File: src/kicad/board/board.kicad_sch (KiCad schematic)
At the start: 20 parts, among them J1 USB_C_Receptacle_USB2.0, J2 Conn_01x06, J3 Micro_SD_Card_Det

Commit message: update, schematic should be done
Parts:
- added H1, H2, H3, H4: MountingHole, MountingHole:MountingHole_3.2mm_M3_DIN965_Pad, symbol Mechanical:MountingHole
- R3, R4, R5, R6, R7, R8: value 47K -> 10K; footprint Resistor_SMD:R_0805_2012Metric -> Resistor_SMD:R_0603_1608Metric; Vendor C17713 -> C25804
- gave numbers to parts that had none: 5
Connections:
- net +3.3V: no longer R5.1
- net GND: now also R5.2
- net SD_CLK: now also R5.1; no longer R5.2
- net SD_DAT2: now reaches J3.1 (DAT2), R8.2
- net SD_DAT1: now reaches J3.8 (DAT1), R3.2
- no-connect marks 16 -> 18
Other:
- moved on the sheet: C1, C2, R3, R4, R5, R6, R7, R8

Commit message: wip
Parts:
- C1: footprint Capacitor_SMD:C_0805_2012Metric -> Capacitor_SMD:C_0603_1608Metric; Vendor C15850 -> C19702
- C2: value 0.1uF -> 100nF; footprint Capacitor_SMD:C_0805_2012Metric -> Capacitor_SMD:C_0603_1608Metric; Vendor C28233 -> C14663
- R1, R2: footprint Resistor_SMD:R_0805_2012Metric -> Resistor_SMD:R_0603_1608Metric; Vendor C27834 -> C23186
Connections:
- net rp2040/GPIO12: now also J2.1 (Pin_1)
- net rp2040/GPIO13: now also J2.2 (Pin_2)
- net rp2040/GPIO14: now also J2.3 (Pin_3)
- net rp2040/GPIO15: now also J2.4 (Pin_4)
- net rp2040/GPIO16: now also J2.5 (Pin_5); no longer J2.1 (Pin_1)
- net rp2040/GPIO17: now also J2.6 (Pin_6); no longer J2.2 (Pin_2)
- net rp2040/GPIO18: no longer J2.3 (Pin_3)
- net rp2040/GPIO19: no longer J2.4 (Pin_4)
- net rp2040/GPIO20: no longer J2.5 (Pin_5)
- net rp2040/GPIO21: no longer J2.6 (Pin_6)
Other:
- sheet Sound ports: added BLCK, DIN, LRCLK; removed none
- moved on the sheet: H1, H2, H3, H4, J2

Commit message: update
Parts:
- C2: footprint Capacitor_SMD:C_0603_1608Metric -> Capacitor_SMD:C_0402_1005Metric; Vendor C14663 -> C307331
- R10, R9: footprint Resistor_SMD:R_0805_2012Metric -> Resistor_SMD:R_0603_1608Metric; Vendor C17594 -> C25190
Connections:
- net rp2040/GPIO12: no longer J2.1 (Pin_1)
- net rp2040/GPIO13: no longer J2.2 (Pin_2)
- net rp2040/GPIO14: no longer J2.3 (Pin_3)
- net rp2040/GPIO15: no longer J2.4 (Pin_4)
- net rp2040/GPIO16: no longer J2.5 (Pin_5)
- net rp2040/GPIO17: no longer J2.6 (Pin_6)
- no-connect marks 18 -> 6
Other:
- moved on the sheet: J2

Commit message: update
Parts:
- removed J2: Conn_01x06, Connector_PinHeader_2.54mm:PinHeader_1x06_P2.54mm_Vertical, symbol Connector_Generic:Conn_01x06
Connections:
- no-connect marks 6 -> 24
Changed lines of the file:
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@@
   (junction (at 77.47 137.16) (diameter 0) (color 0 0 0 0)
   )
+  (no_connect (at 111.76 109.22))
+  (no_connect (at 148.59 58.42))
   (no_connect (at 81.28 173.99))
+  (no_connect (at 111.76 101.6))
   (no_connect (at 129.54 48.26))
+  (no_connect (at 148.59 83.82))
+  (no_connect (at 148.59 81.28))
   (no_connect (at 81.28 176.53))
+  (no_connect (at 111.76 111.76))
+  (no_connect (at 111.76 106.68))
+  (no_connect (at 148.59 63.5))
+  (no_connect (at 111.76 104.14))
+  (no_connect (at 148.59 55.88))
+  (no_connect (at 111.76 99.06))
+  (no_connect (at 148.59 73.66))
+  (no_connect (at 148.59 66.04))
   (no_connect (at 52.07 69.85))
+  (no_connect (at 148.59 78.74))
+  (no_connect (at 148.59 60.96))
+  (no_connect (at 148.59 76.2))
   (no_connect (at 127 48.26))
+  (no_connect (at 148.59 68.58))
   (no_connect (at 52.07 72.39))
+  (no_connect (at 148.59 71.12))
   (wire (pts (xy 106.68 71.12) (xy 111.76 71.12))
     (stroke (width 0) (type default) (color 0 0 0 0))
@@
     (pin "1")
     (pin "2")
-  )
-  (symbol (lib_id "Connector_Generic:Conn_01x06") (at 100.33 110.49 180) (unit 1)
-    (in_bom yes) (on_board yes)
-    (property "Reference" "J2" (id 0) (at 95.25 105.41 0))
-    (property "Value" "Conn_01x06" (id 1) (at 92.71 107.95 0))
-    (property "Footprint" "Connector_PinHeader_2.54mm:PinHeader_1x06_P2.54mm_Vertical" (id 2) (at 100.33 110.49 0)
-      (effects (font (size 1.27 1.27)) hide)
-    )
-    (property "Datasheet" "~" (id 3) (at 100.33 110.49 0)
-      (effects (font (size 1.27 1.27)) hide)
-    )
-    (pin "1")
-    (pin "2")
-    (pin "3")
-    (pin "4")
-    (pin "5")
-    (pin "6")
   )
   (symbol (lib_id "power:+3.3V") (at 195.58 114.3 0) (unit 1)
@@
       (reference "D5") (unit 1) (value "CHARGE_LED") (footprint "LED_SMD:LED_0805_2012Metric")
     )
-    (path "/d540bb9b-d45f-4ddd-b651-2c00d8abffca/7217d876-f1ed-4bca-b991-1e14633870a6"
-      (reference "FB1") (unit 1) (value "Ferrite") (footprint "Library:Ferrite-0805")
-    )
-    (path "/d540bb9b-d45f-4ddd-b651-2c00d8abffca/c0f8ca9a-4e15-418c-8a7f-48417a436431"
-      (reference "FB2") (unit 1) (value "Ferrite") (footprint "Library:Ferrite-0805")
-    )
     (path "/0b29145a-63e8-45a2-940d-9799db9d94f0"
       (reference "H1") (unit 1) (value "MountingHole") (footprint "MountingHole:MountingHole_3.2mm_M3_DIN965_Pad")
@@
       (reference "J1") (unit 1) (value "USB_C_Receptacle_USB2.0") (footprint "Connector_USB:USB_C_Receptacle_G-Switch_GT-USB-7010ASV")
     )
-    (path "/4de2f5e7-d335-4195-9642-413a4a312947"
-      (reference "J2") (unit 1) (value "Conn_01x06") (footprint "Connector_PinHeader_2.54mm:PinHeader_1x06_P2.54mm_Vertical")
-    )
     (path "/6374251b-7a4e-4399-bc11-b4640567a0db"

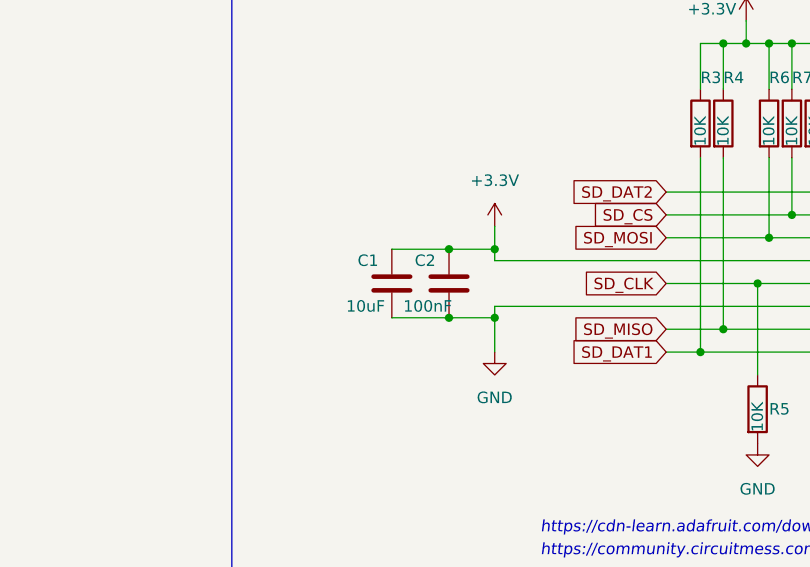
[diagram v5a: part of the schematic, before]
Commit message: separate io board from main
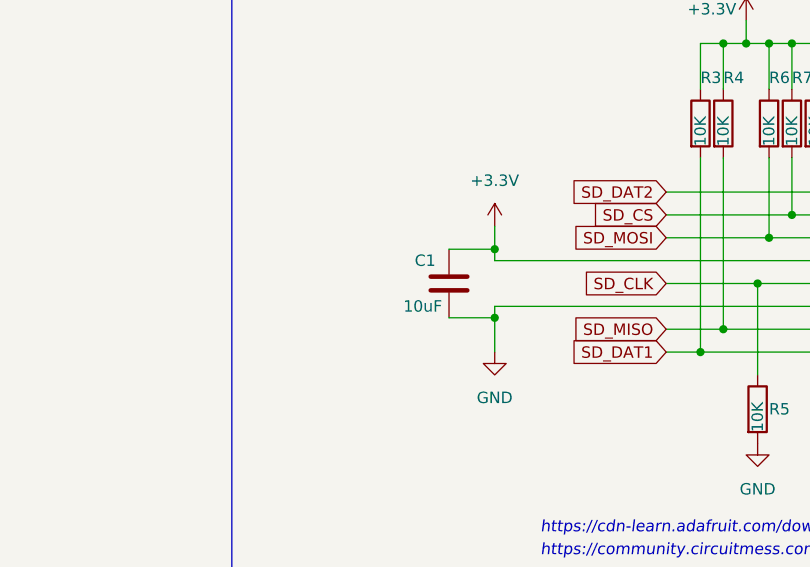
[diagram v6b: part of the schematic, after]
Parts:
- removed C2: 100nF, Capacitor_SMD:C_0402_1005Metric, symbol Device:C
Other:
- moved on the sheet: C1
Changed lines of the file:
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@@
 (kicad_sch (version 20211123) (generator eeschema)
   (paper "A4")
-  (junction (at 39.37 160.02) (diameter 0) (color 0 0 0 0)
-  )
   (junction (at 74.93 81.28) (diameter 0) (color 0 0 0 0)
   )
@@
   )
   (junction (at 29.21 82.55) (diameter 0) (color 0 0 0 0)
-  )
-  (junction (at 39.37 167.64) (diameter 0) (color 0 0 0 0)
   )
   (junction (at 44.45 167.64) (diameter 0) (color 0 0 0 0)
@@
     (stroke (width 0) (type default) (color 0 0 0 0))
   )
-  (wire (pts (xy 33.02 160.02) (xy 39.37 160.02))
-    (stroke (width 0) (type default) (color 0 0 0 0))
-  )
   (wire (pts (xy 93.98 62.23) (xy 111.76 62.23))
     (stroke (width 0) (type default) (color 0 0 0 0))
@@
   )
   (wire (pts (xy 236.22 114.3) (xy 238.76 114.3))
-    (stroke (width 0) (type default) (color 0 0 0 0))
-  )
-  (wire (pts (xy 33.02 167.64) (xy 39.37 167.64))
     (stroke (width 0) (type default) (color 0 0 0 0))
   )
@@
       (effects (font (size 1.27 1.27)) hide)
     )
-  )
-  (symbol (lib_id "Device:C") (at 39.37 163.83 0) (unit 1)
-    (in_bom yes) (on_board yes)
-    (property "Reference" "C2" (id 0) (at 35.56 161.29 0)
-      (effects (font (size 1.27 1.27)) (justify left))
-    )
-    (property "Value" "100nF" (id 1) (at 34.29 166.37 0)
-      (effects (font (size 1.27 1.27)) (justify left))
-    )
-    (property "Footprint" "Capacitor_SMD:C_0402_1005Metric" (id 2) (at 40.3352 167.64 0)
-      (effects (font (size 1.27 1.27)) hide)
-    )
-    (property "Datasheet" "~" (id 3) (at 39.37 163.83 0)
-      (effects (font (size 1.27 1.27)) hide)
-    )
-    (property "Vendor" "C307331" (id 4) (at 39.37 163.83 0)
-      (effects (font (size 1.27 1.27)) hide)
-    )
-    (pin "1")
-    (pin "2")
   )
   (symbol (lib_id "Device:R") (at 73.66 177.8 0) (unit 1)
@@
     (pin "1")
   )
-  (symbol (lib_id "Device:C") (at 33.02 163.83 0) (unit 1)
-    (in_bom yes) (on_board yes)
-    (property "Reference" "C1" (id 0) (at 29.21 161.29 0)
-      (effects (font (size 1.27 1.27)) (justify left))
-    )
-    (property "Value" "10uF" (id 1) (at 27.94 166.37 0)
-      (effects (font (size 1.27 1.27)) (justify left))
-    )
-    (property "Footprint" "Capacitor_SMD:C_0603_1608Metric" (id 2) (at 33.9852 167.64 0)
-      (effects (font (size 1.27 1.27)) hide)
-    )
-    (property "Datasheet" "~" (id 3) (at 33.02 163.83 0)
-      (effects (font (size 1.27 1.27)) hide)
-    )
-    (property "Vendor" "C19702" (id 4) (at 33.02 163.83 0)
+  (symbol (lib_id "Device:C") (at 39.37 163.83 0) (unit 1)
+    (in_bom yes) (on_board yes)
+    (property "Reference" "C1" (id 0) (at 35.56 161.29 0)
+      (effects (font (size 1.27 1.27)) (justify left))
+    )
+    (property "Value" "10uF" (id 1) (at 34.29 166.37 0)
+      (effects (font (size 1.27 1.27)) (justify left))
+    )
+    (property "Footprint" "Capacitor_SMD:C_0603_1608Metric" (id 2) (at 40.3352 167.64 0)
+      (effects (font (size 1.27 1.27)) hide)
+    )
+    (property "Datasheet" "~" (id 3) (at 39.37 163.83 0)
+      (effects (font (size 1.27 1.27)) hide)
+    )
+    (property "Vendor" "C19702" (id 4) (at 39.37 163.83 0)
       (effects (font (size 1.27 1.27)) hide)
     )
@@
       (reference "C1") (unit 1) (value "10uF") (footprint "Capacitor_SMD:C_0603_1608Metric")
     )
-    (path "/1b30703b-465f-4cce-94e8-92560a46498a"
-      (reference "C2") (unit 1) (value "100nF") (footprint "Capacitor_SMD:C_0402_1005Metric")
-    )
     (path "/792c0ba8-28d7-4e30-aff1-9f3fa34c73f6/1dc6a10f-ec56-4ffc-9d20-6da7a3305ac3"

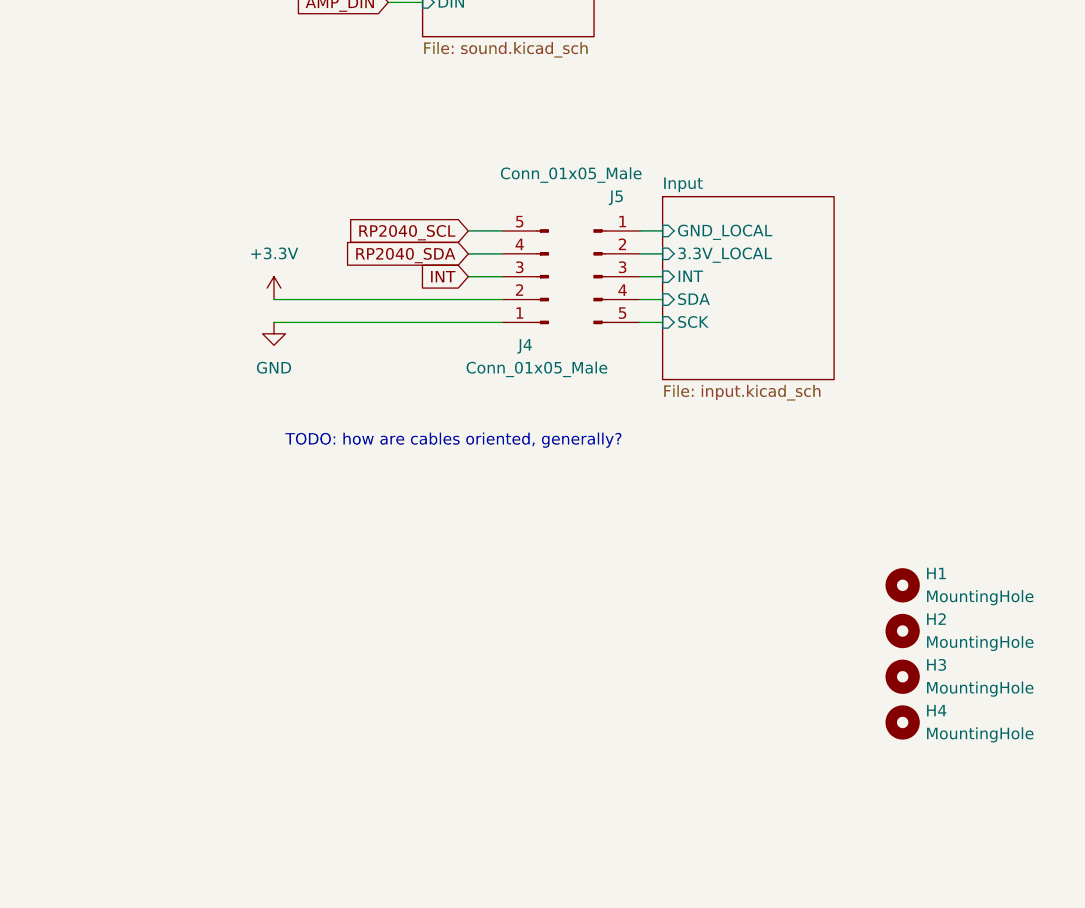
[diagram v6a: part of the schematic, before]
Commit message: remove io-board stuff from the main board project
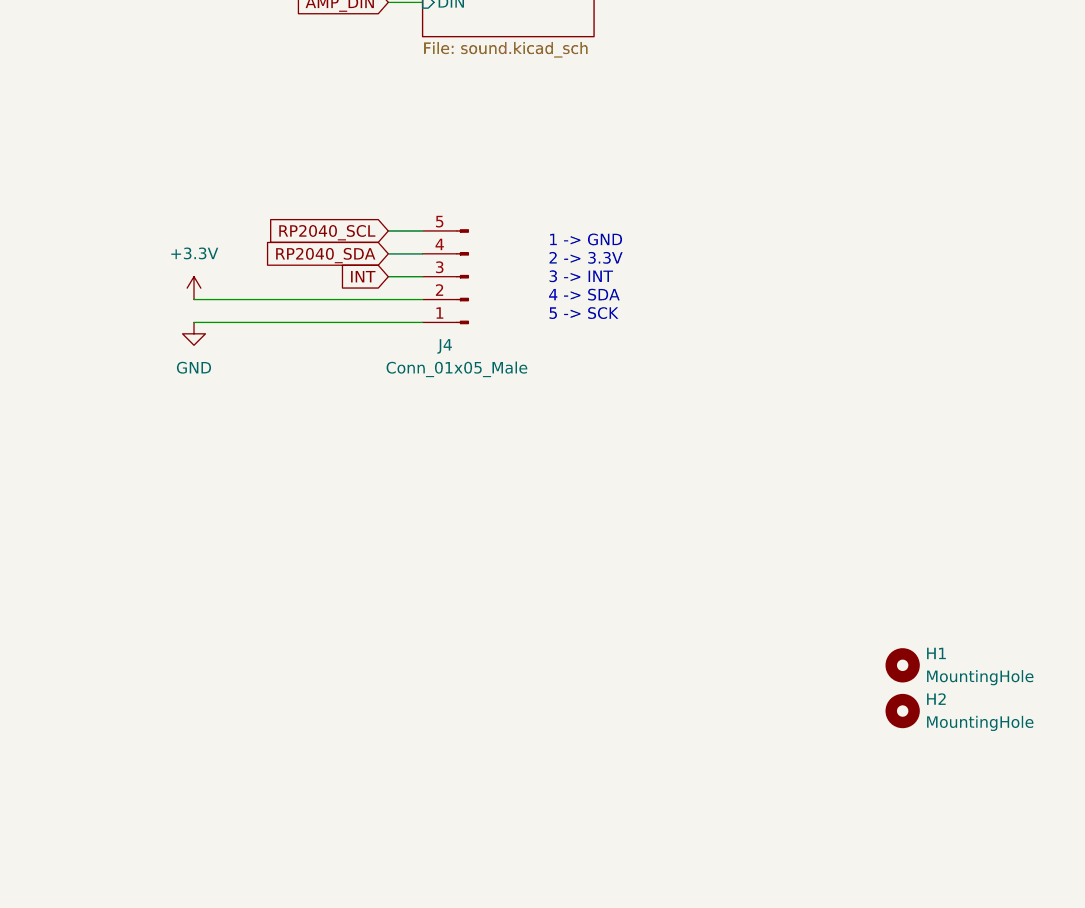
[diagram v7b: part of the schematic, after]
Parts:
- removed H3, H4: MountingHole, MountingHole:MountingHole_3.2mm_M3_DIN965_Pad, symbol Mechanical:MountingHole
- removed J5: Conn_01x05_Male, Connector_JST:JST_PH_B5B-PH-SM4-TB_1x05-1MP_P2.00mm_Vertical, symbol Connector:Conn_01x05_Male
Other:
- removed sheet Input
- note added: "1 -> GND 2 -> 3.3V 3 -> INT 4 -> SDA 5 -> SCK"
- note removed: "TODO: how are cables oriented, generally?"
- moved on the sheet: H1, H2, J4

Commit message: cleanup
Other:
- sheet Power: file power2.kicad_sch -> power.kicad_sch
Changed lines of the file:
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@@
       (effects (font (size 1.27 1.27)) (justify left bottom))
     )
-    (property "Sheet file" "power2.kicad_sch" (id 1) (at 212.09 62.8146 0)
+    (property "Sheet file" "power.kicad_sch" (id 1) (at 212.09 62.8146 0)
       (effects (font (size 1.27 1.27)) (justify left top))
     )
@@
       (reference "#PWR010") (unit 1) (value "GND") (footprint "")
     )
-    (path "/4532e7a8-aa46-45fe-9bdb-5c2c6a438547/8d634ab3-a294-443d-bb98-407e3f0e217e"
-      (reference "#PWR011") (unit 1) (value "GND") (footprint "")
-    )
-    (path "/4532e7a8-aa46-45fe-9bdb-5c2c6a438547/16745edd-e0ff-436e-8a35-1dee71f99778"
-      (reference "#PWR012") (unit 1) (value "GND") (footprint "")
-    )
-    (path "/4532e7a8-aa46-45fe-9bdb-5c2c6a438547/5c05b0ff-52ac-4cbb-a560-b7ac16182c58"
-      (reference "#PWR013") (unit 1) (value "GND") (footprint "")
-    )
-    (path "/4532e7a8-aa46-45fe-9bdb-5c2c6a438547/9ef619b9-7f98-4f18-8e00-4d178f04922b"
-      (reference "#PWR014") (unit 1) (value "GND") (footprint "")
-    )
     (path "/d540bb9b-d45f-4ddd-b651-2c00d8abffca/dd82f178-553c-4d6c-ab4b-61ab073f61bb"
       (reference "#PWR015") (unit 1) (value "GND") (footprint "")
@@
       (reference "#PWR0101") (unit 1) (value "GND") (footprint "")
     )
+    (path "/4532e7a8-aa46-45fe-9bdb-5c2c6a438547/9ef619b9-7f98-4f18-8e00-4d178f04922b"
+      (reference "#PWR0102") (unit 1) (value "GND") (footprint "")
+    )
+    (path "/4532e7a8-aa46-45fe-9bdb-5c2c6a438547/5c05b0ff-52ac-4cbb-a560-b7ac16182c58"
+      (reference "#PWR0103") (unit 1) (value "GND") (footprint "")
+    )
+    (path "/4532e7a8-aa46-45fe-9bdb-5c2c6a438547/16745edd-e0ff-436e-8a35-1dee71f99778"
+      (reference "#PWR0104") (unit 1) (value "GND") (footprint "")
+    )
+    (path "/4532e7a8-aa46-45fe-9bdb-5c2c6a438547/8d634ab3-a294-443d-bb98-407e3f0e217e"
+      (reference "#PWR0105") (unit 1) (value "GND") (footprint "")
+    )
     (path "/4532e7a8-aa46-45fe-9bdb-5c2c6a438547/a4cb6c9b-4536-4020-a9fc-ab93b2a586b8"
